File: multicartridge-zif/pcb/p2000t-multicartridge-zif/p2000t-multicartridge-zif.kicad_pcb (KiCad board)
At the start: 2 copper layers, 80 x 100 mm, 16 parts, among them J1 P2000T_cartridge_edge, SW1 Soft Reset, SW2 SW_DIP_x05, U1 SST39SF040, U2 74HC123, U3 74HC00

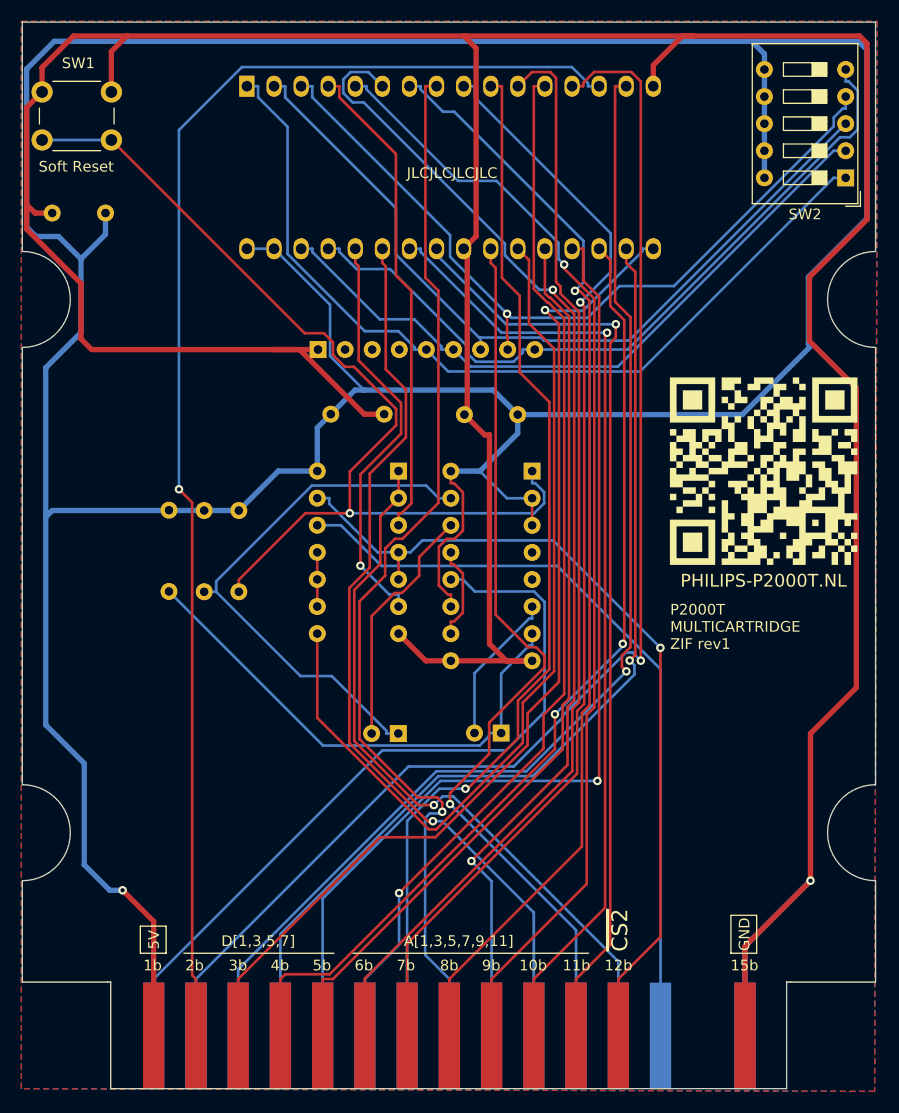
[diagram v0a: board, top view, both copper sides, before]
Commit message: Revision of ZIF cartridge
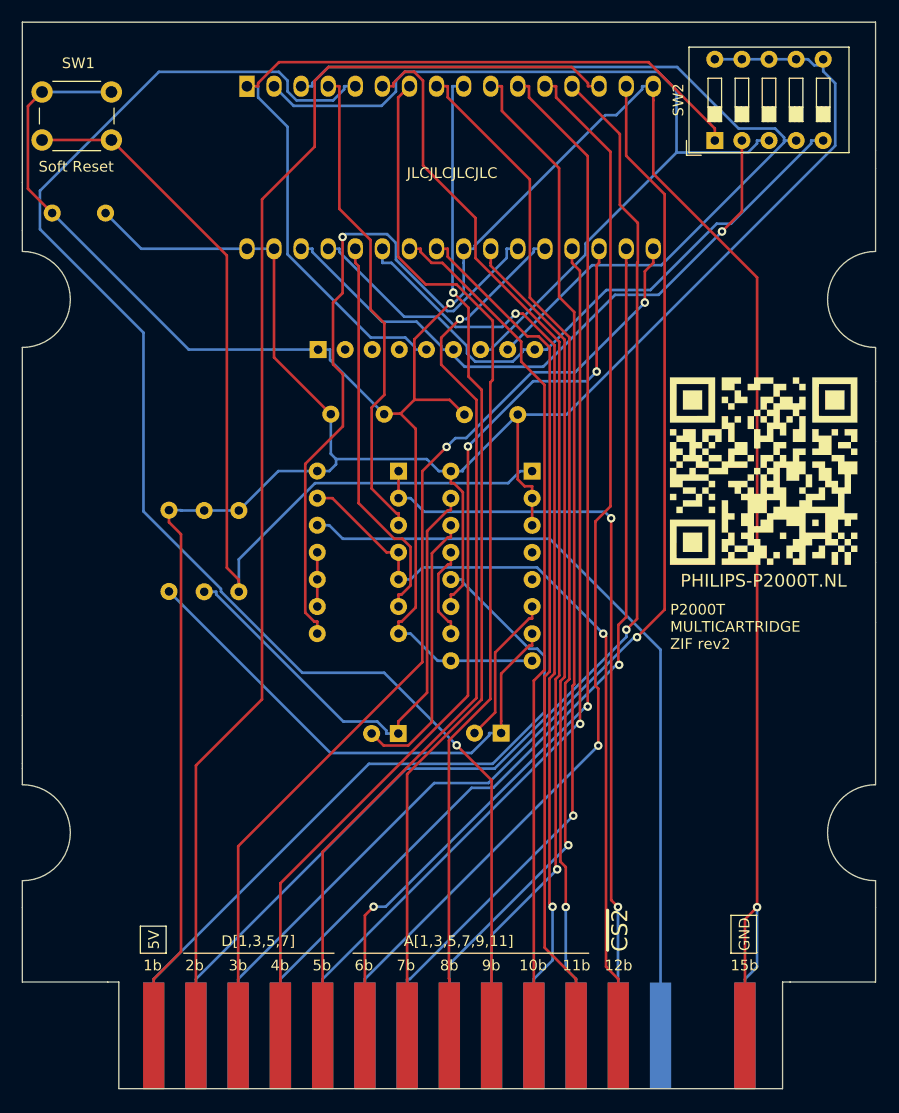
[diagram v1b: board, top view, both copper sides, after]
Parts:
- moved SW2 12.8 mm to (108.1, 55.2), turned to 90 degrees
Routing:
- net +5V: track 364.4 -> 212.3 mm, vias 1 -> 0
- net GND: track 354.1 -> 249.9 mm, vias 1 -> 2
- net A7: track 105.0 -> 137.9 mm
- net ~{CS}: track 83.8 -> 63.4 mm, vias 0 -> 1
- net D6: track 94.8 -> 84.3 mm
- net A9: track 90.7 -> 80.7 mm, vias 1 -> 0
- net A14: track 70.0 -> 60.2 mm
- net A15: track 75.0 -> 84.5 mm, vias 1 -> 0
- net A3: track 103.6 -> 94.1 mm
- net D0: track 122.0 -> 113.6 mm
- net A11: track 88.3 -> 80.8 mm, vias 1 -> 0
- net A10: track 84.9 -> 77.4 mm
- net A5: track 103.6 -> 96.6 mm, vias 1 -> 0
- net ~{CARSEL2}: track 79.8 -> 72.8 mm
- net A16: track 76.2 -> 83.0 mm
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- removed copper zone on B.Cu, net +5V
- removed copper zone on F.Cu, net GND
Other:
- outline, holes or cut-outs redrawn
- board text added: "P2000T MULTICARTRIDGE ZIF rev2"
- board text removed: "P2000T MULTICARTRIDGE ZIF rev1"
